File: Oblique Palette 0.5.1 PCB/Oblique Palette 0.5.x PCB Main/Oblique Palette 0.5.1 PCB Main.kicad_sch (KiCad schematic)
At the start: 20 parts, among them J11 Conn_01x03_Male_Pin, J13 Conn_01x03_Male_Pin, J14 Conn_01x03_Male_Pin, J2 Conn_01x03_Male_Pin, J4 Conn_01x03_Male_Pin, J5 Conn_01x03_Male_Pin, J7 Conn_01x03_Male_Pin, J71 Conn_01x03_Male_Pin, J72 Conn_01x02_Pin, J9 Conn_01x03_Male_Pin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

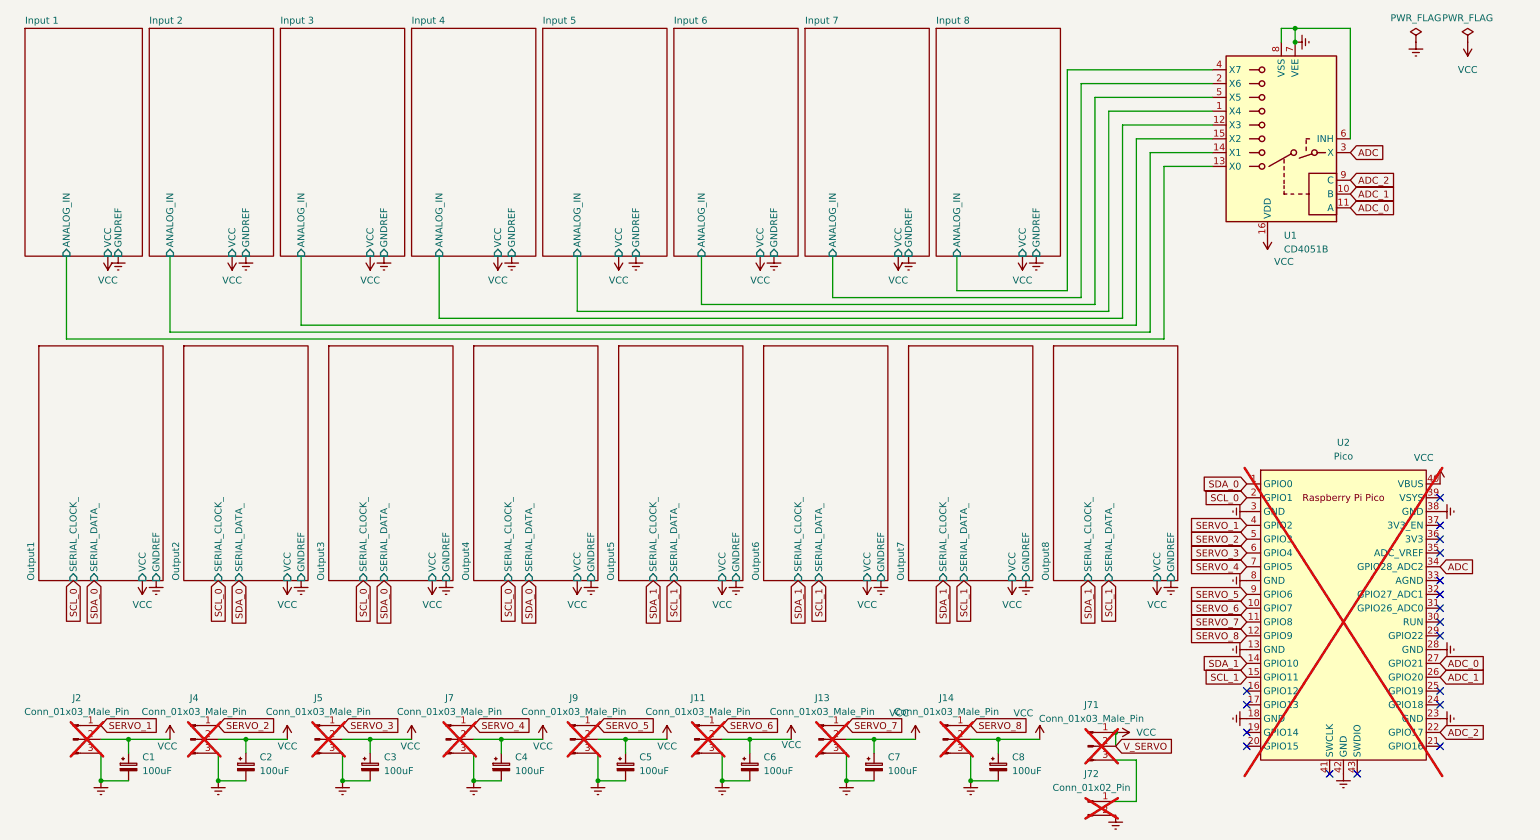
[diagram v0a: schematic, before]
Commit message: More input and output channel corrections
Reduced the white LED inputs to have a range of 0V:3.3V to get a greater range of brightness across the range of values

Powered the input op amps from 3v3 so we can't blow up. Changed the comparison voltage for the LEDs to 0V:3.3V instead of up to 5 so brightnesses are consistent between input and output channels.
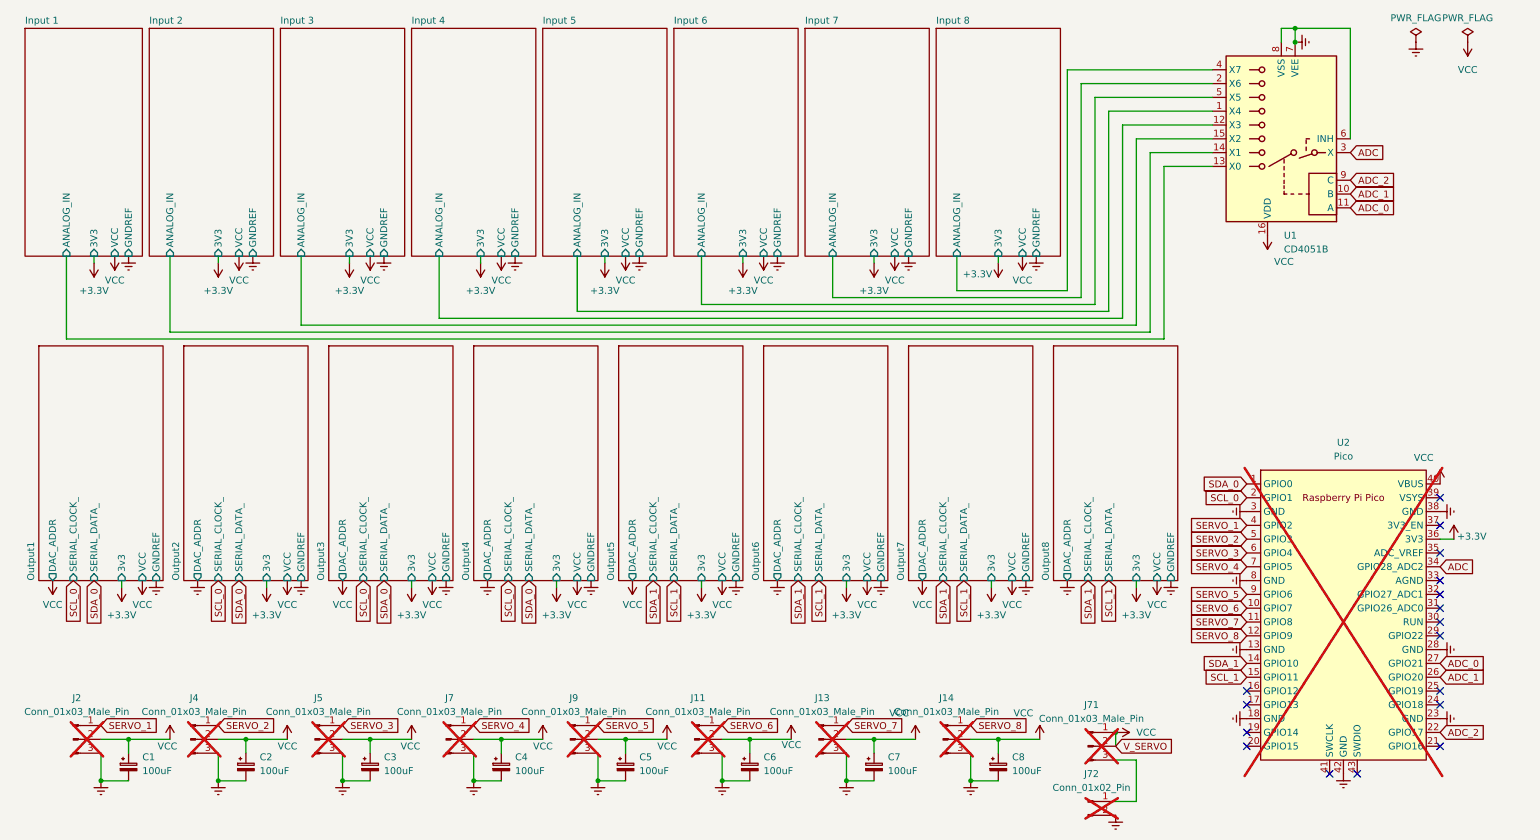
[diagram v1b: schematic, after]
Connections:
- net +3.3V: now reaches U2.36 (3V3)
- no-connect marks 18 -> 17
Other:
- sheet Input 1 ports: added 3V3; removed none
- sheet Input 2 ports: added 3V3; removed none
- sheet Input 3 ports: added 3V3; removed none
- sheet Input 4 ports: added 3V3; removed none
- sheet Input 5 ports: added 3V3; removed none
- sheet Input 6 ports: added 3V3; removed none
- sheet Input 7 ports: added 3V3; removed none
- sheet Input 8 ports: added 3V3; removed none
- sheet Output1 ports: added 3v3, DAC_ADDR; removed none
- sheet Output2 ports: added 3v3, DAC_ADDR; removed none
- sheet Output3 ports: added 3v3, DAC_ADDR; removed none
- sheet Output4 ports: added 3v3, DAC_ADDR; removed none
- sheet Output5 ports: added 3v3, DAC_ADDR; removed none
- sheet Output6 ports: added 3v3, DAC_ADDR; removed none
- sheet Output7 ports: added 3v3, DAC_ADDR; removed none
- sheet Output8 ports: added 3v3, DAC_ADDR; removed none

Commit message: Front panel channel labels
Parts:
- J11, J13, J14, J2, J4, J5, J7, J71, J9: now fitted
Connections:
- net ADC: no longer U2.34 (GPIO28_ADC2)
- new net ANALOG_PIN: U2.34 (GPIO28_ADC2)
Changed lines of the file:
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@@
 		)
 	)
-	(global_label "ADC"
+	(global_label "ANALOG_PIN"
 		(shape input)
 		(at 274.32 115.57 0)
@@
 		)
 		(property "Intersheetrefs" "${INTERSHEET_REFS}"
-			(at 280.9338 115.57 0)
+			(at 288.6144 115.57 0)
 			(effects
 				(font
@@
 	(symbol
 		(lib_id "power:GNDREF")
-		(at 45.72 118.11 0)
+		(at 19.05 118.11 0)
 		(unit 1)
 		(exclude_from_sim no)
@@
 		(fields_autoplaced yes)
 		(property "Reference" "#PWR0343"
-			(at 45.72 124.46 0)
+			(at 19.05 124.46 0)
 			(effects
 				(font
@@
 		)
 		(property "Value" "GNDREF"
-			(at 45.72 123.19 0)
+			(at 19.05 123.19 0)
 			(effects
 				(font
@@
 		)
 		(property "Footprint" ""
-			(at 45.72 118.11 0)
+			(at 19.05 118.11 0)
 			(effects
 				(font
@@
 		)
 		(property "Datasheet" ""
-			(at 45.72 118.11 0)
+			(at 19.05 118.11 0)
 			(effects
 				(font
@@
 		)
 		(property "Description" "Power symbol creates a global label with name \"GNDREF\" , reference supply ground"
-			(at 45.72 118.11 0)
+			(at 19.05 118.11 0)
 			(effects
 				(font
@@
 		(in_bom yes)
 		(on_board yes)
-		(dnp yes)
+		(dnp no)
 		(property "Reference" "J4"
 			(at 45.085 139.7 0)
@@
 	(symbol
 		(lib_id "power:VCC")
-		(at 125.73 118.11 180)
+		(at 99.06 118.11 180)
 		(unit 1)
 		(exclude_from_sim no)
@@
 		(fields_autoplaced yes)
 		(property "Reference" "#PWR0342"
-			(at 125.73 114.3 0)
+			(at 99.06 114.3 0)
 			(effects
 				(font
@@
 		)
 		(property "Value" "VCC"
-			(at 125.73 122.555 0)
+			(at 99.06 122.555 0)
 			(effects
 				(font
@@
 		)
 		(property "Footprint" ""
-			(at 125.73 118.11 0)
+			(at 99.06 118.11 0)
 			(effects
 				(font
@@
 		)
 		(property "Datasheet" ""
-			(at 125.73 118.11 0)
+			(at 99.06 118.11 0)
 			(effects
 				(font
@@
 		)
 		(property "Description" "Power symbol creates a global label with name \"VCC\""
-			(at 125.73 118.11 0)
+			(at 99.06 118.11 0)
 			(effects
 				(font
@@
 		(in_bom yes)
 		(on_board yes)
-		(dnp yes)
+		(dnp no)
 		(property "Reference" "J2"
 			(at 23.495 139.7 0)
@@
 	(symbol
 		(lib_id "power:GNDREF")
-		(at 152.4 118.11 0)
+		(at 125.73 118.11 0)
 		(unit 1)
 		(exclude_from_sim no)
@@
 		(fields_autoplaced yes)
 		(property "Reference" "#PWR0338"
-			(at 152.4 124.46 0)
+			(at 125.73 124.46 0)
 			(effects
 				(font
@@
 		)
 		(property "Value" "GNDREF"
-			(at 152.4 123.19 0)
+			(at 125.73 123.19 0)
 			(effects
 				(font
@@
 		)
 		(property "Footprint" ""
-			(at 152.4 118.11 0)
+			(at 125.73 118.11 0)
 			(effects
 				(font
@@
 		)
 		(property "Datasheet" ""
-			(at 152.4 118.11 0)
+			(at 125.73 118.11 0)
 			(effects
 				(font
@@
 		)
 		(property "Description" "Power symbol creates a global label with name \"GNDREF\" , reference supply ground"
-			(at 152.4 118.11 0)
+			(at 125.73 118.11 0)
 			(effects
 				(font
@@
 		(in_bom yes)
 		(on_board yes)
-		(dnp yes)
+		(dnp no)
 		(property "Reference" "J7"
 			(at 92.075 139.7 0)
@@
 		(in_bom yes)
 		(on_board yes)
-		(dnp yes)
+		(dnp no)
 		(property "Reference" "J5"
 			(at 67.945 139.7 0)
@@
 	(symbol
 		(lib_id "power:VCC")
-		(at 72.39 118.11 180)
+		(at 45.72 118.11 180)
 		(unit 1)
 		(exclude_from_sim no)
@@
 		(on_board yes)
 		(dnp no)
-		(fields_autoplaced yes)
 		(property "Reference" "#PWR0340"
-			(at 72.39 114.3 0)
+			(at 45.72 114.3 0)
 			(effects
 				(font
@@
 		)
 		(property "Value" "VCC"
-			(at 72.39 122.555 0)
+			(at 45.72 122.555 0)
 			(effects
 				(font
@@
 		)
 		(property "Footprint" ""
-			(at 72.39 118.11 0)
+			(at 45.72 118.11 0)
 			(effects
 				(font
@@
 		)
 		(property "Datasheet" ""
-			(at 72.39 118.11 0)
+			(at 45.72 118.11 0)
 			(effects
 				(font
@@
 		)
 		(property "Description" "Power symbol creates a global label with name \"VCC\""
-			(at 72.39 118.11 0)
+			(at 45.72 118.11 0)
 			(effects
 				(font
@@
 		(in_bom yes)
 		(on_board yes)
-		(dnp yes)
+		(dnp no)
 		(property "Reference" "J11"
 			(at 137.795 139.7 0)
@@
 		(in_bom yes)
 		(on_board yes)
-		(dnp yes)
+		(dnp no)
 		(property "Reference" "J13"
 			(at 160.655 139.7 0)
@@
 		(in_bom yes)
 		(on_board yes)
-		(dnp yes)
+		(dnp no)
 		(property "Reference" "J14"
 			(at 183.515 139.7 0)
@@
 	(symbol
 		(lib_id "power:VCC")
-		(at 19.05 118.11 180)
+		(at 205.74 118.11 180)
 		(unit 1)
 		(exclude_from_sim no)
@@
 		(fields_autoplaced yes)
 		(property "Reference" "#PWR0339"
-			(at 19.05 114.3 0)
+			(at 205.74 114.3 0)
 			(effects
 				(font
@@
 		)
 		(property "Value" "VCC"
-			(at 19.05 122.555 0)
+			(at 205.74 122.555 0)
 			(effects
 				(font
@@
 		)
 		(property "Footprint" ""
-			(at 19.05 118.11 0)
+			(at 205.74 118.11 0)
 			(effects
 				(font
@@
 		)
 		(property "Datasheet" ""
-			(at 19.05 118.11 0)
+			(at 205.74 118.11 0)
 			(effects
 				(font
@@
 		)
 		(property "Description" "Power symbol creates a global label with name \"VCC\""
-			(at 19.05 118.11 0)
+			(at 205.74 118.11 0)
 			(effects
 				(font
@@
 	(symbol
 		(lib_id "power:VCC")
-		(at 179.07 118.11 180)
+		(at 152.4 118.11 180)
 		(unit 1)
 		(exclude_from_sim no)
@@
 		(fields_autoplaced yes)
 		(property "Reference" "#PWR0344"
-			(at 179.07 114.3 0)
+			(at 152.4 114.3 0)
 			(effects
 				(font
@@
 		)
 		(property "Value" "VCC"
-			(at 179.07 122.555 0)
+			(at 152.4 122.555 0)
 			(effects
 				(font
@@
 		)
 		(property "Footprint" ""
-			(at 179.07 118.11 0)
+			(at 152.4 118.11 0)
 			(effects
 				(font
@@
 		)
 		(property "Datasheet" ""
-			(at 179.07 118.11 0)
+			(at 152.4 118.11 0)
 			(effects
 				(font
@@
 		)
 		(property "Description" "Power symbol creates a global label with name \"VCC\""
-			(at 179.07 118.11 0)
+			(at 152.4 118.11 0)
 			(effects
 				(font
@@
 	(symbol
 		(lib_id "power:GNDREF")
-		(at 205.74 118.11 0)
+		(at 179.07 118.11 0)
 		(unit 1)
 		(exclude_from_sim no)
@@
 		(fields_autoplaced yes)
 		(property "Reference" "#PWR0337"
-			(at 205.74 124.46 0)
+			(at 179.07 124.46 0)
 			(effects
 				(font
@@
 		)
 		(property "Value" "GNDREF"
-			(at 205.74 123.19 0)
+			(at 179.07 123.19 0)
 			(effects
 				(font
@@
 		)
 		(property "Footprint" ""
-			(at 205.74 118.11 0)
+			(at 179.07 118.11 0)
 			(effects
 				(font
@@
 		)
 		(property "Datasheet" ""
-			(at 205.74 118.11 0)
+			(at 179.07 118.11 0)
 			(effects
 				(font
@@
 		)
 		(property "Description" "Power symbol creates a global label with name \"GNDREF\" , reference supply ground"
-			(at 205.74 118.11 0)
+			(at 179.07 118.11 0)
 			(effects
 				(font
@@
 		(in_bom yes)
 		(on_board yes)
-		(dnp yes)
+		(dnp no)
 		(property "Reference" "J9"
 			(at 114.935 139.7 0)
@@
 	(symbol
 		(lib_id "power:GNDREF")
-		(at 99.06 118.11 0)
+		(at 72.39 118.11 0)
 		(unit 1)
 		(exclude_from_sim no)
@@
 		(fields_autoplaced yes)
 		(property "Reference" "#PWR0341"
-			(at 99.06 124.46 0)
+			(at 72.39 124.46 0)
 			(effects
 				(font
@@
 		)
 		(property "Value" "GNDREF"
-			(at 99.06 123.19 0)
+			(at 72.39 123.19 0)
 			(effects
 				(font
@@
 		)
 		(property "Footprint" ""
-			(at 99.06 118.11 0)
+			(at 72.39 118.11 0)
 			(effects
 				(font
@@
 		)
 		(property "Datasheet" ""
-			(at 99.06 118.11 0)
+			(at 72.39 118.11 0)
 			(effects
 				(font
@@
 		)
 		(property "Description" "Power symbol creates a global label with name \"GNDREF\" , reference supply ground"
-			(at 99.06 118.11 0)
+			(at 72.39 118.11 0)
 			(effects
 				(font
@@
 		(in_bom yes)
 		(on_board yes)
-		(dnp yes)
+		(dnp no)
 		(property "Reference" "J71"
 			(at 210.185 140.97 0)

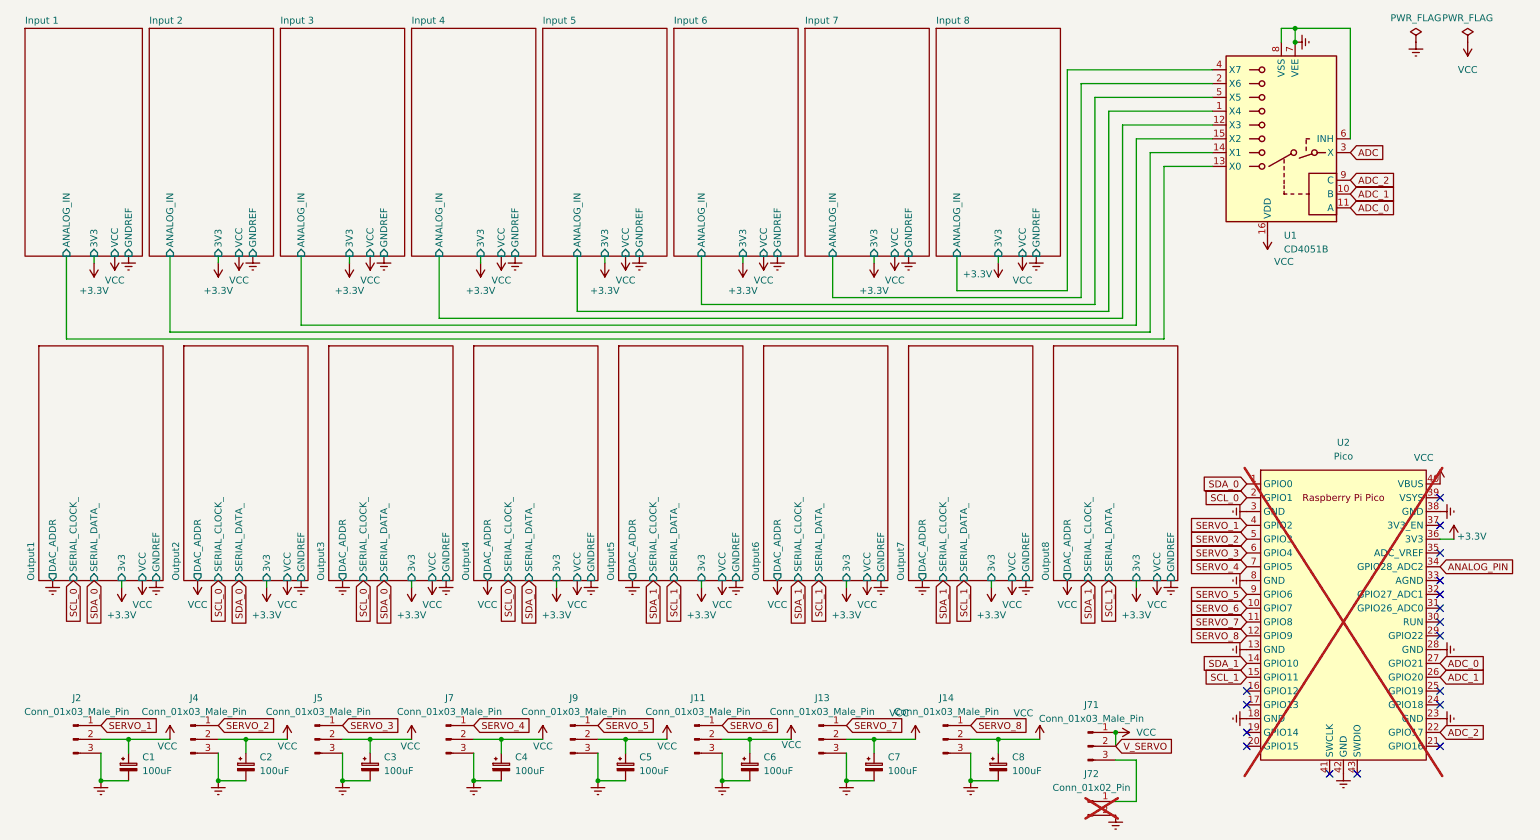
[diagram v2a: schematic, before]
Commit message: Fixing input channels
Issues:
1. Some (all?) input channels are not connected to the multiplexer. This seems to be an issue with my hierarchical labels?
2. Input op amps do not seem to have inputs for the yellow and red LEDs. Again, they seem to be disconnected.

Checked: levels coming out of the potentiometers are correct.
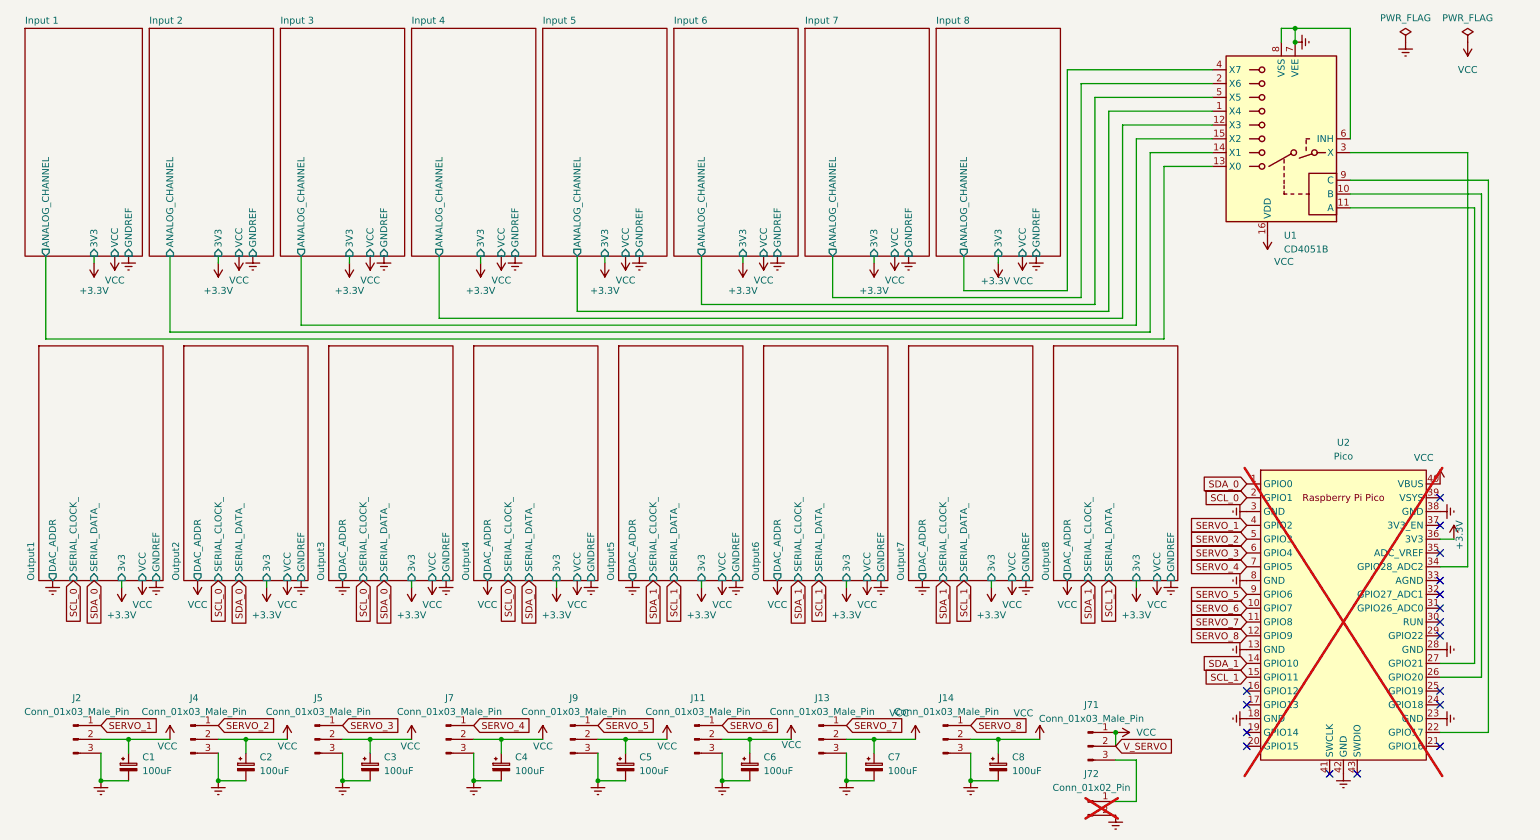
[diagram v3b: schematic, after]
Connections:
- net ANALOG_PIN is gone; now on an unnamed net: U2.34 (GPIO28_ADC2)
- net ADC: no longer names the net of U1.3 (X)
- net ADC_0: no longer names the net of U1.11 (A), U2.27 (GPIO21)
- net ADC_1: no longer names the net of U1.10 (B), U2.26 (GPIO20)
- net ADC_2: no longer names the net of U1.9 (C), U2.22 (GPIO17)
- net Input 1/ANALOG_IN renamed Input 1/ANALOG_CHANNEL
- net Input 2/ANALOG_IN renamed Input 2/ANALOG_CHANNEL
- net Input 3/ANALOG_IN renamed Input 3/ANALOG_CHANNEL
- net Input 4/ANALOG_IN renamed Input 4/ANALOG_CHANNEL
- net Input 5/ANALOG_IN renamed Input 5/ANALOG_CHANNEL
- net Input 6/ANALOG_IN renamed Input 6/ANALOG_CHANNEL
- net Input 7/ANALOG_IN renamed Input 7/ANALOG_CHANNEL
- net Input 8/ANALOG_IN renamed Input 8/ANALOG_CHANNEL
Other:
- sheet Input 1 ports: added ANALOG_CHANNEL; removed ANALOG_IN
- sheet Input 2 ports: added ANALOG_CHANNEL; removed ANALOG_IN
- sheet Input 3 ports: added ANALOG_CHANNEL; removed ANALOG_IN
- sheet Input 4 ports: added ANALOG_CHANNEL; removed ANALOG_IN
- sheet Input 5 ports: added ANALOG_CHANNEL; removed ANALOG_IN
- sheet Input 6 ports: added ANALOG_CHANNEL; removed ANALOG_IN
- sheet Input 7 ports: added ANALOG_CHANNEL; removed ANALOG_IN
- sheet Input 8 ports: added ANALOG_CHANNEL; removed ANALOG_IN

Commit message: All traces connected. Replaced caps with 1mF SMD ones to add muffling power for and to the servos.
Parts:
- removed J71: Conn_01x03_Male_Pin, Connector_PinHeader_2.54mm:PinHeader_1x03_P2.54mm_Vertical, symbol Connector:Conn_01x03_Pin
- removed J72: Conn_01x02_Pin, Connector_PinHeader_2.54mm:PinHeader_1x02_P2.54mm_Vertical, symbol Connector:Conn_01x02_Pin
- C1, C2, C3, C4, C5, C6, C7, C8: value 100uF -> 1mF
